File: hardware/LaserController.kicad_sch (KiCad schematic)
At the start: 3 parts, among them J37 TEC Driver, J38 LD Driver, SW1 SW_DPST_x2

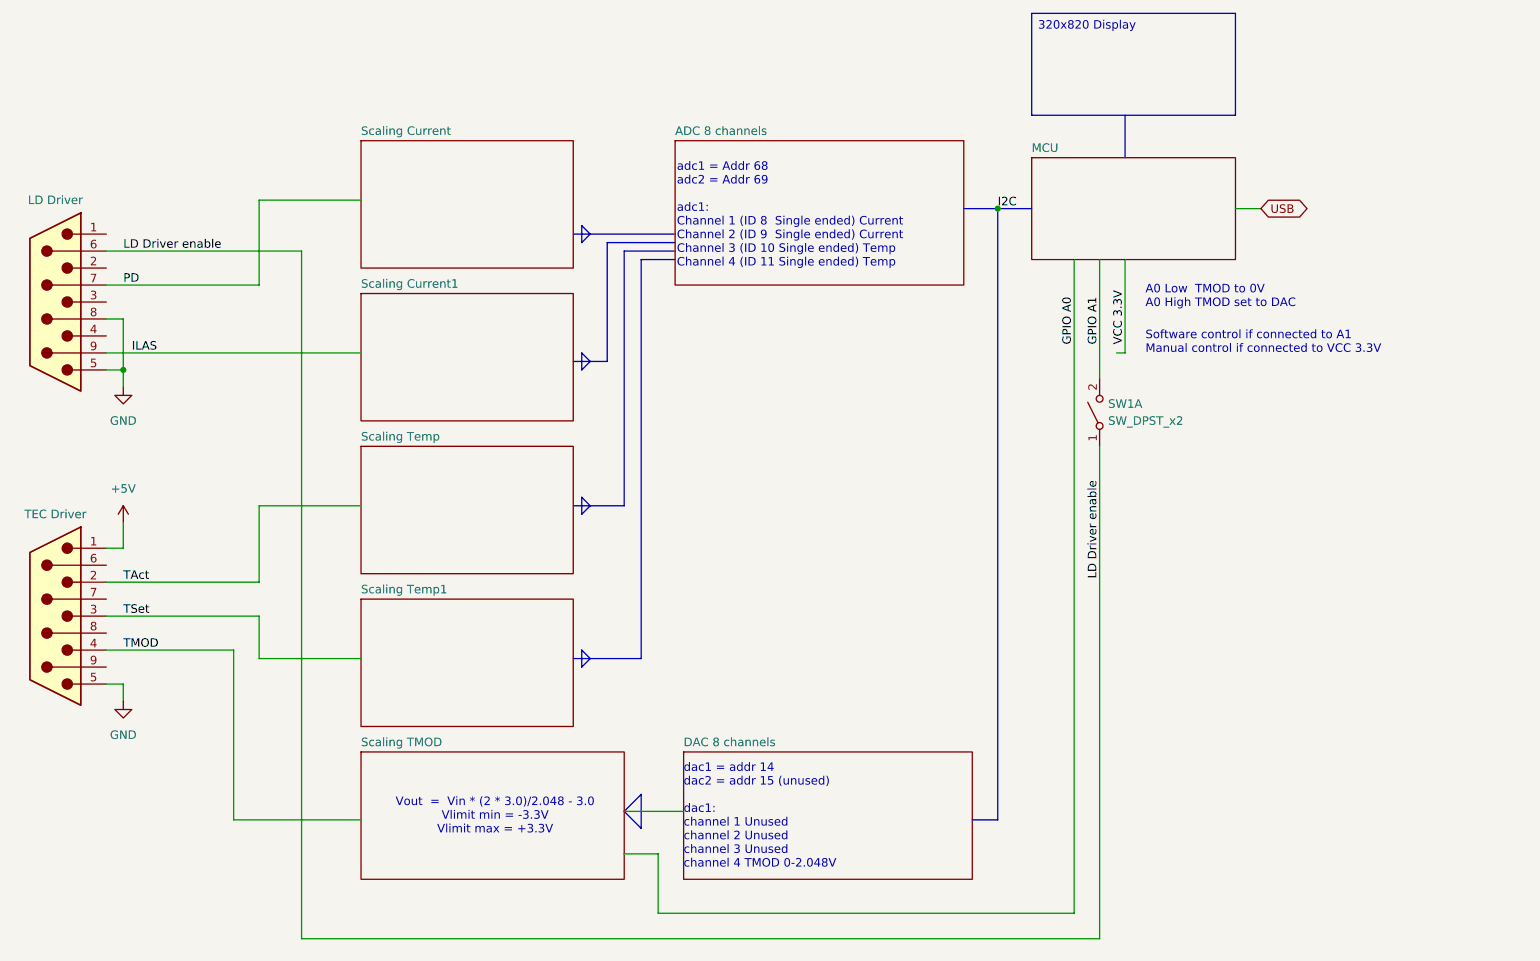
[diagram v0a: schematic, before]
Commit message: Diagram added for laser Controller
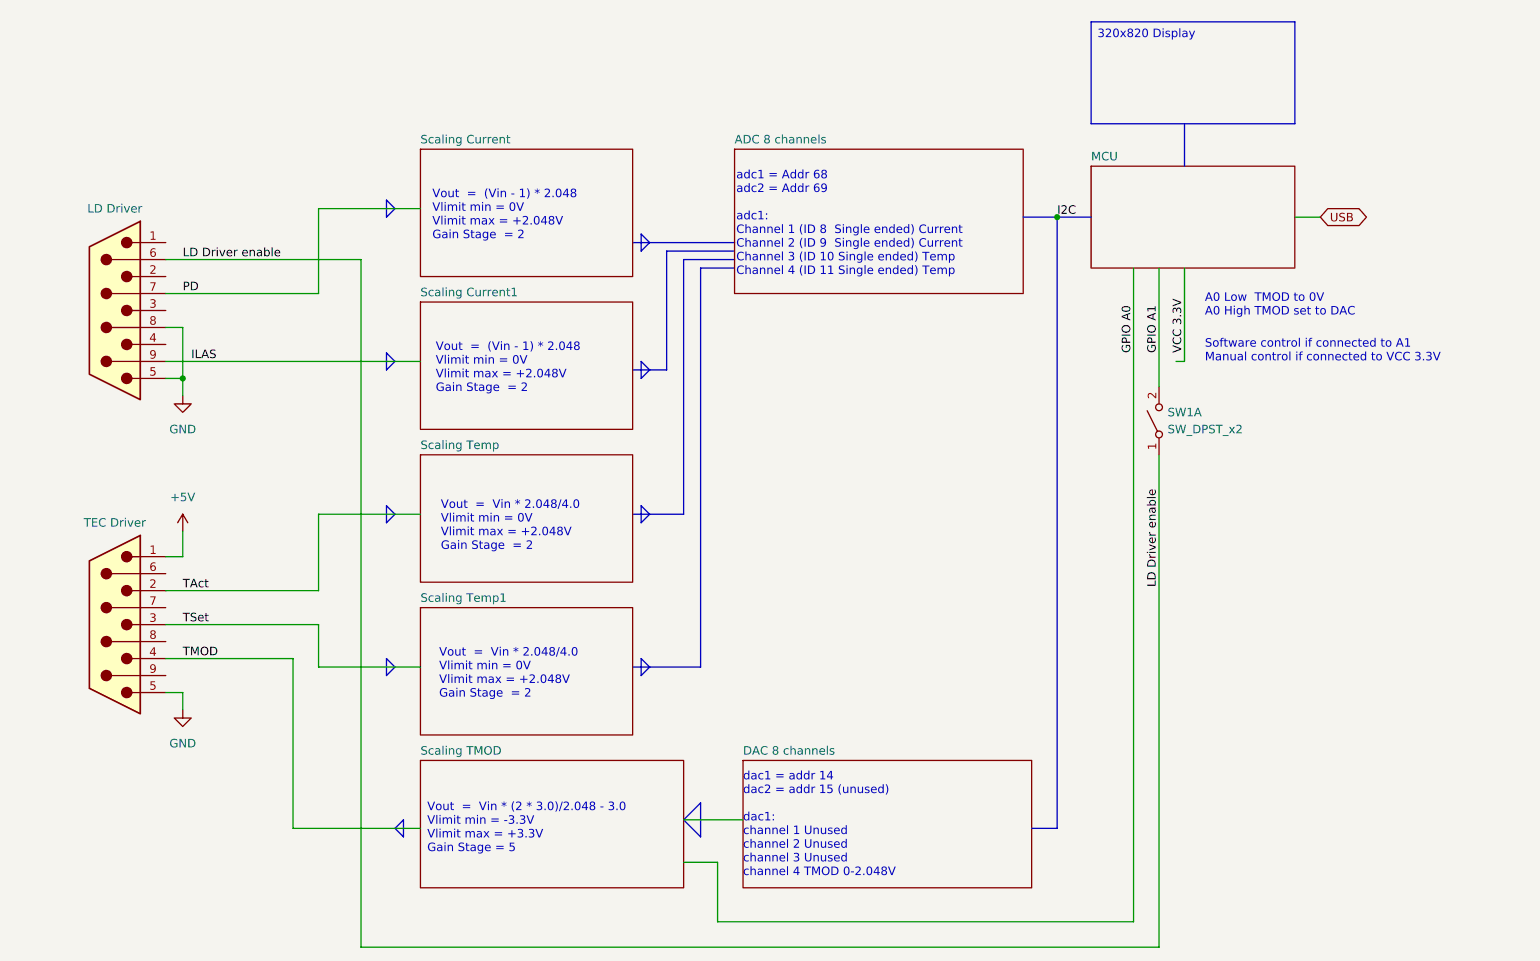
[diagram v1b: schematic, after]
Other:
- note added: "Vout = (Vin - 1) * 2.048 Vlimit min = 0V Vlimit max = +2.048V Gain Stage = 2"
- note added: "Vout = Vin * (2 * 3.0)/2.048 - 3.0 Vlimit min = -3.3V Vlimit max = +3.3V Gain Stage = 5"
- note added: "Vout = Vin * 2.048/4.0 Vlimit min = 0V Vlimit max = +2.048V Gain Stage = 2"
- note removed: "Vout = Vin * (2 * 3.0)/2.048 - 3.0 Vlimit min = -3.3V Vlimit max = +3.3V"
- moved on the sheet: SW1A
